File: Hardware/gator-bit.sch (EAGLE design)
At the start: 82 parts, among them J19 GATOR, J2 GATOR, J20 GATOR, J21 GATOR, J22 GATOR, J25 GATOR, J28 GATOR, J3 GATOR, J32 GATOR, J33 GATOR, J34 GATOR, J35 GATOR, J36 GATOR, J39 GATOR, J4 GATOR, J40 GATOR, U2 micro:bit, U4 MIC5219 3.3V

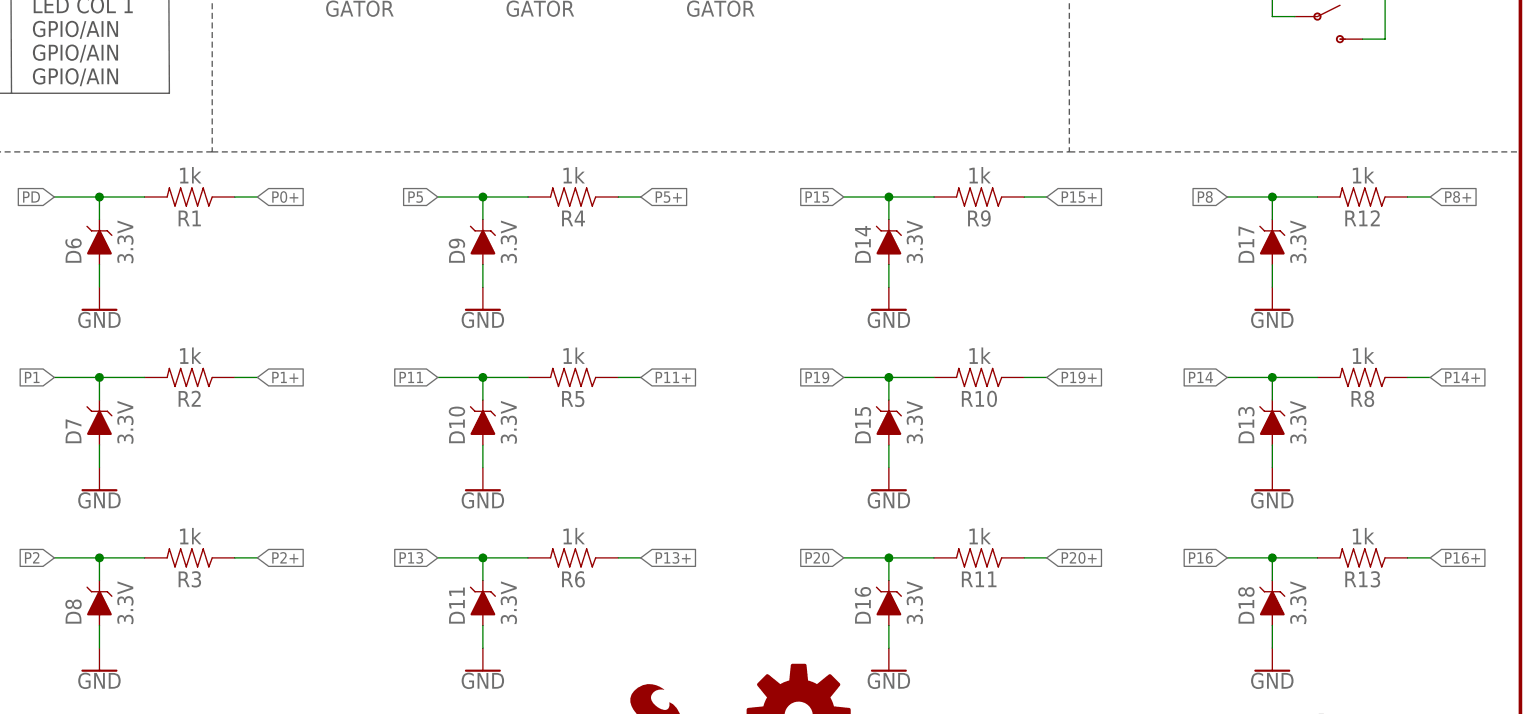
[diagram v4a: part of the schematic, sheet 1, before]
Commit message: updating resistor values
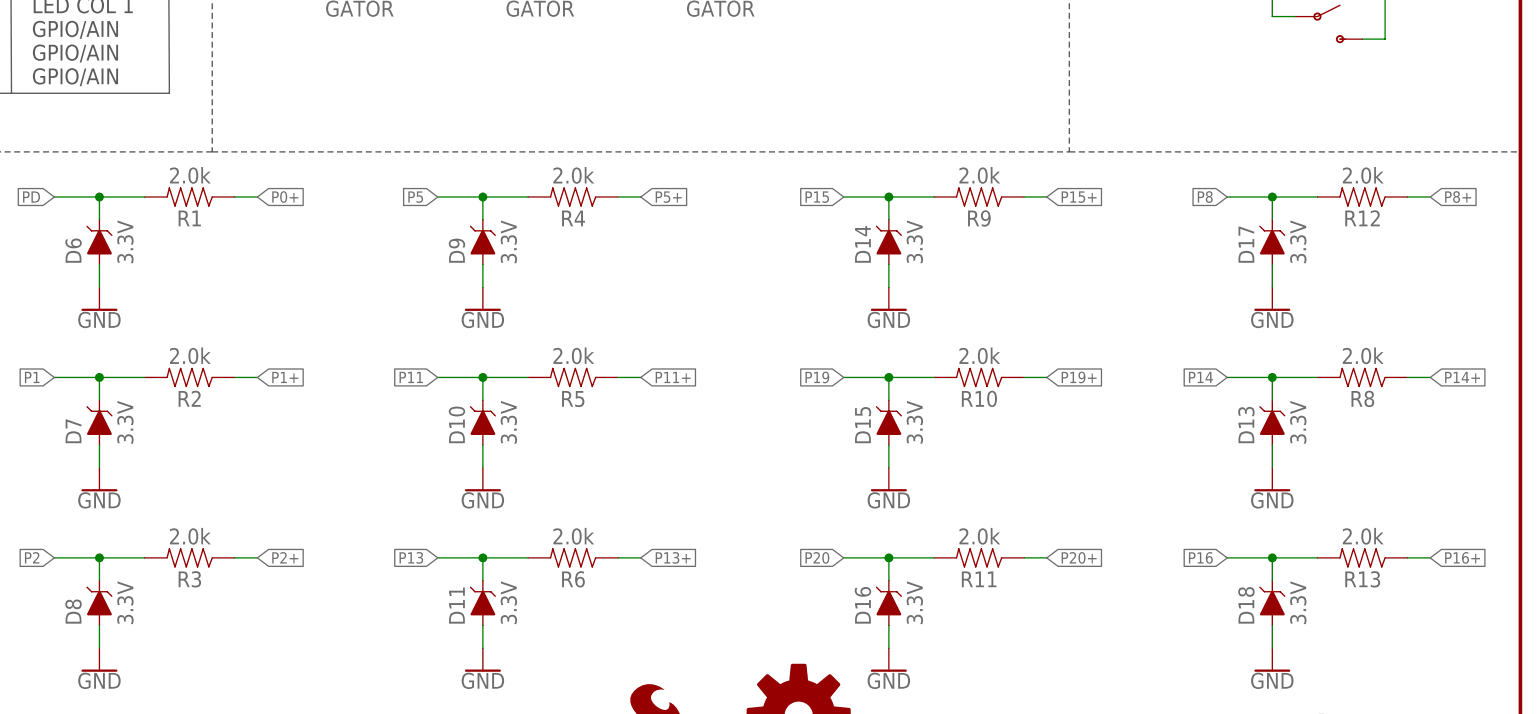
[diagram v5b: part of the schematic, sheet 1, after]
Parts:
- R1, R10, R11, R12, R13, R2, R3, R4, R5, R6, R8, R9: value 1k -> 2.0k; device SparkFun-Resistors:1KOHM-0603-1/10W-1% -> SparkFun-Resistors:2.0KOHM-0603-1/10W-5%
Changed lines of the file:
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@@
 <part name="LS1" library="SparkFun-Electromechanical" deviceset="BUZZER" device="-SMD"/>
 <part name="D6" library="SparkFun-DiscreteSemi" deviceset="DIODE-ZENER" device="-MM3Z3V3T1G" value="3.3V"/>
-<part name="R1" library="SparkFun-Resistors" deviceset="1KOHM" device="-0603-1/10W-1%" value="1k"/>
+<part name="R1" library="SparkFun-Resistors" deviceset="2.0KOHM" device="-0603-1/10W-5%" value="2.0k"/>
 <part name="S2" library="SparkFun-Switches" deviceset="SWITCH-SPDT" device="-SMD-AYZ0202"/>
 <part name="S3" library="SparkFun-Switches" deviceset="SWITCH-SPDT" device="-SMD-AYZ0202"/>
@@
 <part name="GND7" library="SparkFun-PowerSymbols" deviceset="GND" device=""/>
 <part name="D7" library="SparkFun-DiscreteSemi" deviceset="DIODE-ZENER" device="-MM3Z3V3T1G" value="3.3V"/>
-<part name="R2" library="SparkFun-Resistors" deviceset="1KOHM" device="-0603-1/10W-1%" value="1k"/>
+<part name="R2" library="SparkFun-Resistors" deviceset="2.0KOHM" device="-0603-1/10W-5%" value="2.0k"/>
 <part name="GND8" library="SparkFun-PowerSymbols" deviceset="GND" device=""/>
 <part name="D8" library="SparkFun-DiscreteSemi" deviceset="DIODE-ZENER" device="-MM3Z3V3T1G" value="3.3V"/>
-<part name="R3" library="SparkFun-Resistors" deviceset="1KOHM" device="-0603-1/10W-1%" value="1k"/>
+<part name="R3" library="SparkFun-Resistors" deviceset="2.0KOHM" device="-0603-1/10W-5%" value="2.0k"/>
 <part name="GND9" library="SparkFun-PowerSymbols" deviceset="GND" device=""/>
 <part name="D9" library="SparkFun-DiscreteSemi" deviceset="DIODE-ZENER" device="-MM3Z3V3T1G" value="3.3V"/>
-<part name="R4" library="SparkFun-Resistors" deviceset="1KOHM" device="-0603-1/10W-1%" value="1k"/>
+<part name="R4" library="SparkFun-Resistors" deviceset="2.0KOHM" device="-0603-1/10W-5%" value="2.0k"/>
 <part name="GND10" library="SparkFun-PowerSymbols" deviceset="GND" device=""/>
 <part name="D10" library="SparkFun-DiscreteSemi" deviceset="DIODE-ZENER" device="-MM3Z3V3T1G" value="3.3V"/>
-<part name="R5" library="SparkFun-Resistors" deviceset="1KOHM" device="-0603-1/10W-1%" value="1k"/>
+<part name="R5" library="SparkFun-Resistors" deviceset="2.0KOHM" device="-0603-1/10W-5%" value="2.0k"/>
 <part name="GND11" library="SparkFun-PowerSymbols" deviceset="GND" device=""/>
 <part name="D11" library="SparkFun-DiscreteSemi" deviceset="DIODE-ZENER" device="-MM3Z3V3T1G" value="3.3V"/>
-<part name="R6" library="SparkFun-Resistors" deviceset="1KOHM" device="-0603-1/10W-1%" value="1k"/>
+<part name="R6" library="SparkFun-Resistors" deviceset="2.0KOHM" device="-0603-1/10W-5%" value="2.0k"/>
 <part name="GND12" library="SparkFun-PowerSymbols" deviceset="GND" device=""/>
 <part name="D13" library="SparkFun-DiscreteSemi" deviceset="DIODE-ZENER" device="-MM3Z3V3T1G" value="3.3V"/>
-<part name="R8" library="SparkFun-Resistors" deviceset="1KOHM" device="-0603-1/10W-1%" value="1k"/>
+<part name="R8" library="SparkFun-Resistors" deviceset="2.0KOHM" device="-0603-1/10W-5%" value="2.0k"/>
 <part name="GND14" library="SparkFun-PowerSymbols" deviceset="GND" device=""/>
 <part name="D14" library="SparkFun-DiscreteSemi" deviceset="DIODE-ZENER" device="-MM3Z3V3T1G" value="3.3V"/>
-<part name="R9" library="SparkFun-Resistors" deviceset="1KOHM" device="-0603-1/10W-1%" value="1k"/>
+<part name="R9" library="SparkFun-Resistors" deviceset="2.0KOHM" device="-0603-1/10W-5%" value="2.0k"/>
 <part name="GND15" library="SparkFun-PowerSymbols" deviceset="GND" device=""/>
 <part name="D15" library="SparkFun-DiscreteSemi" deviceset="DIODE-ZENER" device="-MM3Z3V3T1G" value="3.3V"/>
-<part name="R10" library="SparkFun-Resistors" deviceset="1KOHM" device="-0603-1/10W-1%" value="1k"/>
+<part name="R10" library="SparkFun-Resistors" deviceset="2.0KOHM" device="-0603-1/10W-5%" value="2.0k"/>
 <part name="GND16" library="SparkFun-PowerSymbols" deviceset="GND" device=""/>
 <part name="D16" library="SparkFun-DiscreteSemi" deviceset="DIODE-ZENER" device="-MM3Z3V3T1G" value="3.3V"/>
-<part name="R11" library="SparkFun-Resistors" deviceset="1KOHM" device="-0603-1/10W-1%" value="1k"/>
+<part name="R11" library="SparkFun-Resistors" deviceset="2.0KOHM" device="-0603-1/10W-5%" value="2.0k"/>
 <part name="GND17" library="SparkFun-PowerSymbols" deviceset="GND" device=""/>
 <part name="D17" library="SparkFun-DiscreteSemi" deviceset="DIODE-ZENER" device="-MM3Z3V3T1G" value="3.3V"/>
-<part name="R12" library="SparkFun-Resistors" deviceset="1KOHM" device="-0603-1/10W-1%" value="1k"/>
+<part name="R12" library="SparkFun-Resistors" deviceset="2.0KOHM" device="-0603-1/10W-5%" value="2.0k"/>
 <part name="GND18" library="SparkFun-PowerSymbols" deviceset="GND" device=""/>
 <part name="C1" library="SparkFun-Capacitors" deviceset="0.1UF" device="-0603-25V-(+80/-20%)" value="0.1uF"/>
@@
 <part name="J14" library="SparkFun-Connectors" deviceset="CONN_01" device=""/>
 <part name="D18" library="SparkFun-DiscreteSemi" deviceset="DIODE-ZENER" device="-MM3Z3V3T1G" value="3.3V"/>
-<part name="R13" library="SparkFun-Resistors" deviceset="1KOHM" device="-0603-1/10W-1%" value="1k"/>
+<part name="R13" library="SparkFun-Resistors" deviceset="2.0KOHM" device="-0603-1/10W-5%" value="2.0k"/>
 <part name="GND22" library="SparkFun-PowerSymbols" deviceset="GND" device=""/>
 <part name="U4" library="SparkFun-IC-Power" deviceset="V_REG_MIC5219" device="3.3V" value="MIC5219 3.3V"/>

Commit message: Updating file
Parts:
- removed D11, D13, D14, D15, D16: 3.3V, SparkFun-DiscreteSemi:DIODE-ZENER-MM3Z3V3T1G
- removed FD3: FIDUCIAL1X2, SparkFun-Aesthetics:FIDUCIAL1X2
- removed H1, H2, H3, H4: STAND-OFF, SparkFun-Electromechanical:STAND-OFF
- removed J10, J11, J12, J13, J14, J5, J6, J7, J8, J9: (no value), SparkFun-Connectors:CONN_01
- removed R10, R11, R6, R8, R9: 2.0k, SparkFun-Resistors:2.0KOHM-0603-1/10W-5%
- D7: value 3.3V -> 3.6V; device SparkFun-DiscreteSemi:DIODE-ZENER-MM3Z3V3T1G -> SparkFun-DiscreteSemi:DIODE-ZENER-BZT52C3V6S
- LOGO2: value OSHW-LOGOM -> OSHW-LOGOL; device SparkFun-Aesthetics:OSHW-LOGOM -> SparkFun-Aesthetics:OSHW-LOGOL
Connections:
- removed net P13+: J14.1, J32.P$1, R6.1
- removed net P14+: J13.1, J33.P$1, R8.1
- removed net P15+: J12.1, J34.P$1, R9.1
- removed net P19+: J11.1, J36.P$1, R10.1
- removed net P20+: J10.1, J39.P$1, R11.1
- net GND: no longer D11.A, D13.A, D14.A, D15.A, D16.A
- net P13: now also J32.P$1; no longer D11.C, J9.1, R6.2
- net P14: now also J33.P$1; no longer D13.C, J8.1, R8.2
- net P15: now also J34.P$1; no longer D14.C, J7.1, R9.2
- net P19: now also J36.P$1; no longer D15.C, J6.1, R10.2
- net P20: now also J39.P$1; no longer D16.C, J5.1, R11.2
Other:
- moved on the sheet: D17, D18, R12, R13

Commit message: Updating Design Files
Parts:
- removed D10, D17, D8, D9: 3.3V, SparkFun-DiscreteSemi:DIODE-ZENER-MM3Z3V3T1G
- removed D7: 3.6V, SparkFun-DiscreteSemi:DIODE-ZENER-BZT52C3V6S
- removed R12, R5: 2.0k, SparkFun-Resistors:2.0KOHM-0603-1/10W-5%
- removed U4: MIC5219 3.3V, SparkFun-IC-Power:V_REG_MIC52193.3V
- added C6: 10uF, SparkFun-Capacitors:10UF-0603-6.3V-20%
- added D11, D12, D13, D14, D15, D16, D20, D21, D22, D23, D24, D25: 3.3V, SparkFun-DiscreteSemi:DIODE-ZENER-MM3Z3V3T1G
- added R10, R14, R16, R18, R20, R6, R8: 910, SparkFun-Resistors:910OHMOHMS-0603-1/10W-1%
- added R11, R15, R17, R19, R7, R9: 604, SparkFun-Resistors:600OHMOHMS-0603-1/10W-1%
- added U1: TPS63070, SparkFun-IC-Power:TPS63070RNM
- C7: device SparkFun-Capacitors:10UF-POLAR-0603-6.3V-20%(TANT) -> SparkFun-Capacitors:10UF-0603-6.3V-20%
- C9: value 10uF -> 47uF; device SparkFun-Capacitors:10UF-POLAR-0603-6.3V-20%(TANT) -> SparkFun-Capacitors:47UF20%-6.3V-0805
- R1, R4: value 2.0k -> 100k; device SparkFun-Resistors:2.0KOHM-0603-1/10W-5% -> SparkFun-Resistors:100KOHM-0603-1/10W-1%
- R13: value 2.0k -> 604; device SparkFun-Resistors:2.0KOHM-0603-1/10W-5% -> SparkFun-Resistors:600OHMOHMS-0603-1/10W-1%
- R2: value 2.0k -> 10.2K; device SparkFun-Resistors:2.0KOHM-0603-1/10W-5% -> SparkFun-Resistors:10.2KOHM
- R3: value 2.0k -> 274K; device SparkFun-Resistors:2.0KOHM-0603-1/10W-5% -> SparkFun-Resistors:274KOHMOHMS-0603-1/10W-1%
- renumbered D6 to D19
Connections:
- new net PP0: D16.C, D19.A, R11.2, R14.2
- new net PP1: D20.C, D21.A, R15.2, R16.2
- new net PP11: D14.C, D15.A, R10.2, R9.2
- new net PP16: D11.A, D18.C, R13.2, R6.2
- new net PP2: D22.C, D23.A, R17.2, R18.2
- new net PP5: D24.C, D25.A, R19.2, R20.2
- new net PP8: D12.C, D13.A, R7.2, R8.2
- net 3.3V: now also D11.C, D13.C, D15.C, D19.C, D21.C, D23.C, D25.C; no longer C7.+, C8.1, U4.OUT
- net GND: now also D12.A, D14.A, D16.A, D20.A, D22.A, D24.A; no longer C7.-, C8.2, C9.-, D10.A, D17.A, D19.A, D7.A, D8.A, D9.A, U4.GND
- net P0: now also R14.1
- net P0+: now also R11.1; no longer R1.1
- net P1: now also R16.1; no longer D7.C, R2.2
- net P1+: now also R15.1; no longer R2.1
- net P11: now also R10.1; no longer D10.C, R5.2
- net P11+: now also R9.1; no longer R5.1
- net P16: now also R6.1; no longer D18.C, R13.2
- net P2: now also R18.1; no longer D8.C, R3.2
- net P2+: now also R17.1; no longer R3.1
- net P5: now also R20.1; no longer D9.C, R4.2
- net P5+: now also R19.1; no longer R4.1
- net P8: now also R8.1; no longer D17.C, R12.2
- net P8+: now also R7.1; no longer R12.1
- net PD: no longer D19.C, R1.2
- net VIN: no longer C9.+, U4.EN, U4.IN
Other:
- note removed: "3.3V Rail"
- note removed: "VIN 3V-12V"
- moved on the sheet: C8, D18, R13
